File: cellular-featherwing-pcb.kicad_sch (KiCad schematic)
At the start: 65 parts, among them J1 SIM8060-6-0-14-00-A, J2 TSM-116-01-L-SV, J3 TSM-112-01-L-SV, J4 U.FL-R-SMT, U1 BG96, U2 TPS63020QDSJTQ1, U3 TXB0108RGYR, U4 MAX8868EUK30+T

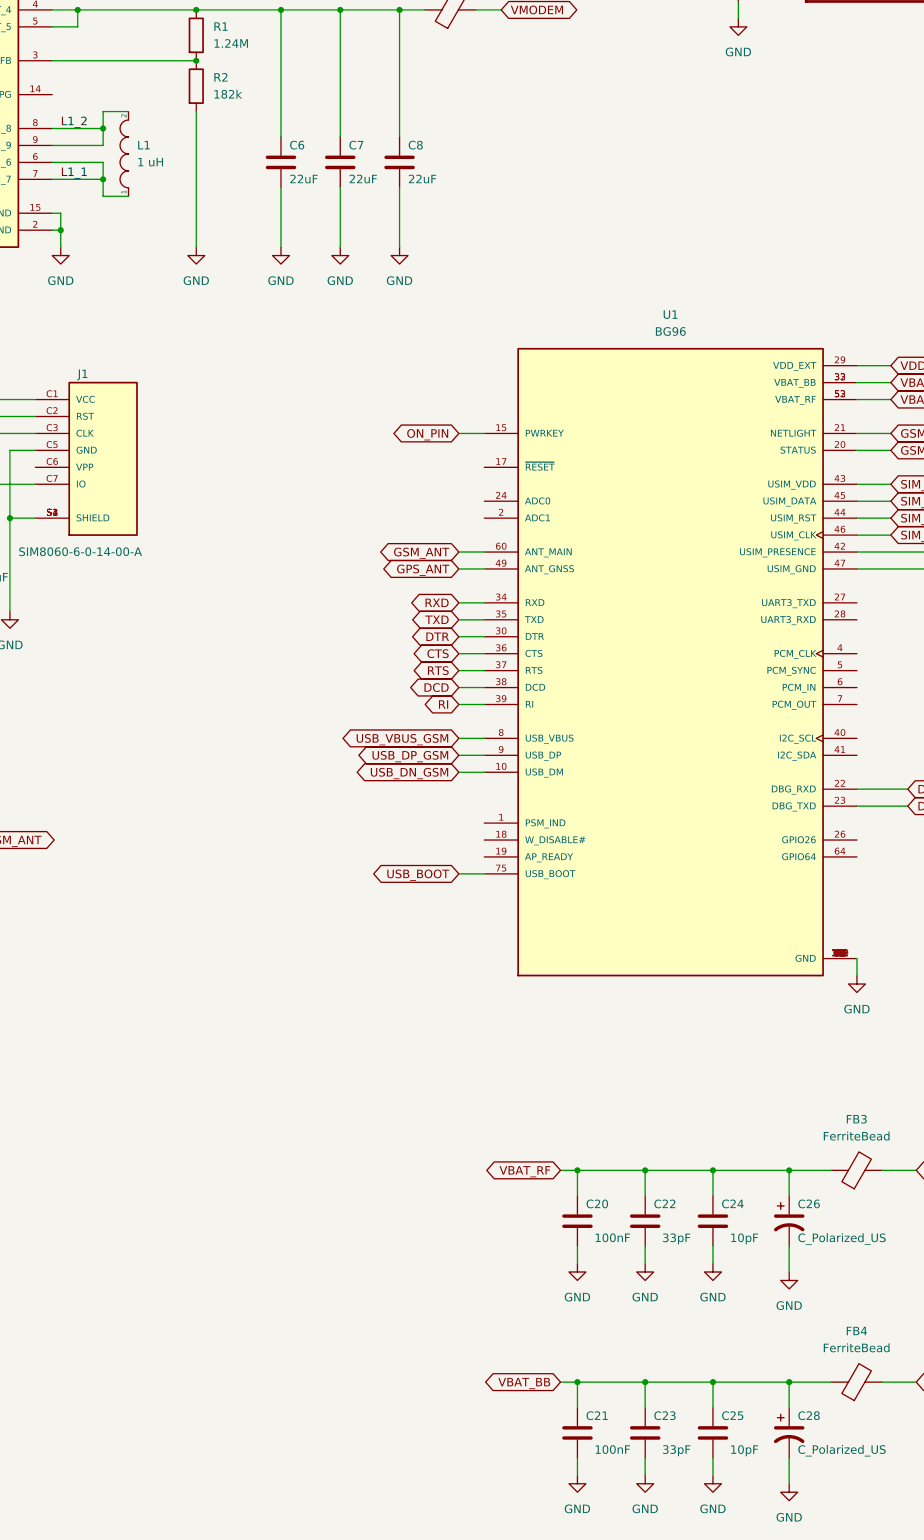
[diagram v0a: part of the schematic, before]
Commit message: Update to kicad 10
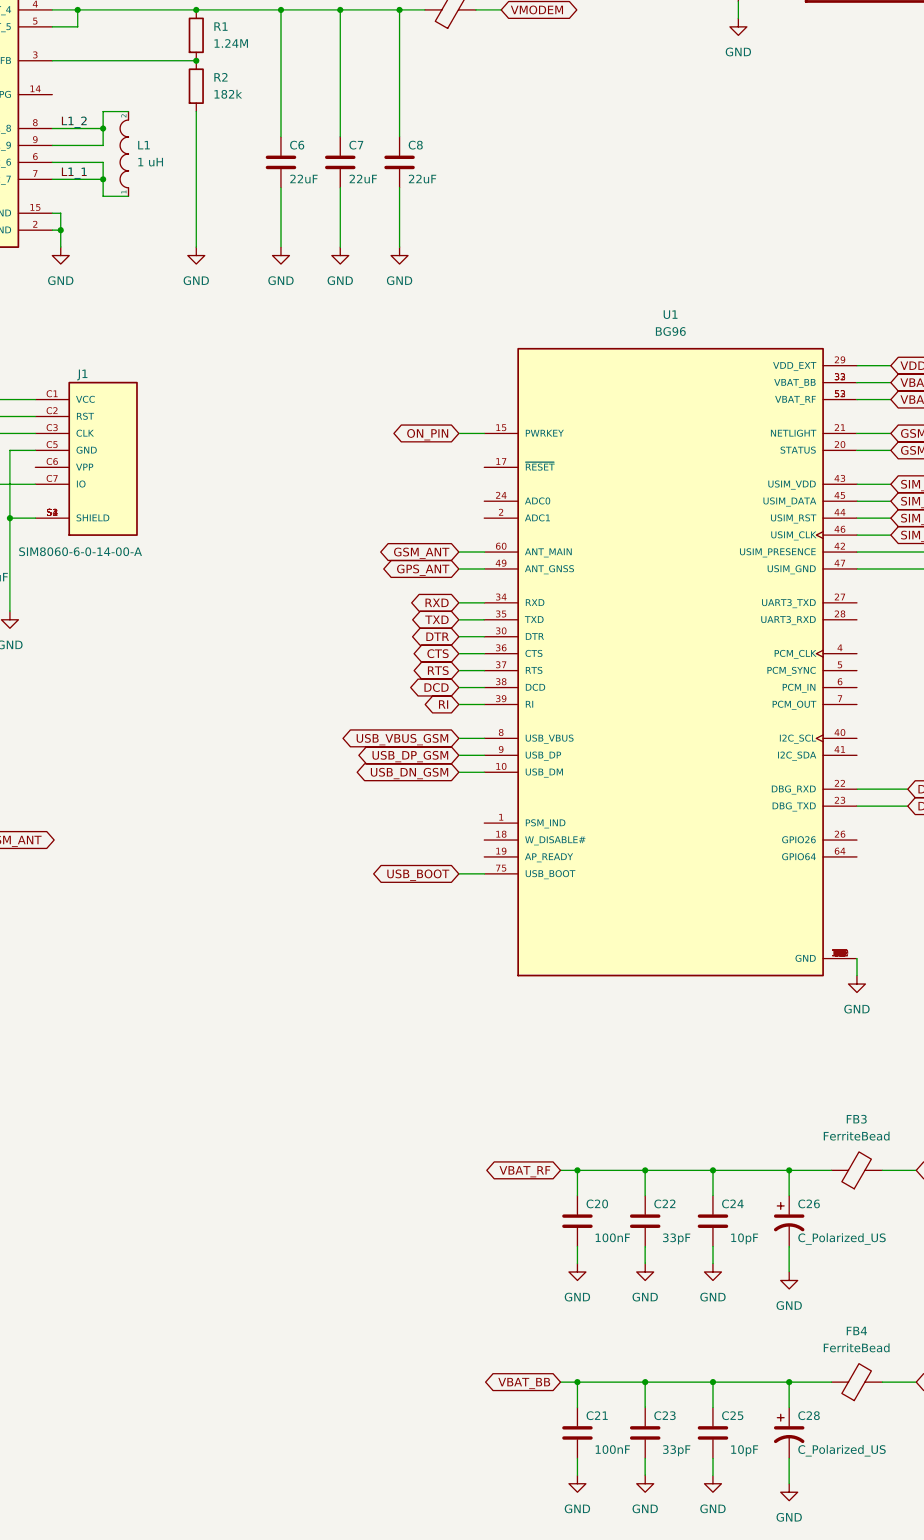
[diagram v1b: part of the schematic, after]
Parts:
- J1: DESCRIPTION SIM8060 is a hinged Sim Card Connector. With 6 contacts, wi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 -> (none)
- J4: DESCRIPTION U.FL Series 50 Ohm Receptacle Male Pins Ultra Small SMT Coa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 -> (none)
